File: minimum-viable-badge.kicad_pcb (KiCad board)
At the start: 2 copper layers, 120 x 64 mm, 67 parts, among them J101 EDGE_CONNECTOR, P101 USB, P102 BATTERY, P103 POT_LONG, P104 BUTTON_A, P105 BUTTON_B, P106 POT_SHORT, P107 MECH, P108 MECH, P109 MECH, P301 eInk, Q101 S8050, Q102 S8050, Q201 FDN340P, Q301 IRLML0030TRPBF, SW101 PRGM, SW102 RESET, SW201 ON|OFF, U101 ESP32-WROOM, U102 CP2102, U201 MCP73831, U202 NCP5501

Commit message: Flipped is better.
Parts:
- C101, C102, C103, C104, C105, C106, C107, C201, C202, C203, C204, C301, C302, C303, C304, C305, C306, C307, C308, C309, C310, C311, C312, D101, D201, D202, D203, D301, D302, D303, F101, J101, L301, P101, P102, P107, P108, P109, P301, Q101, Q102, Q201, Q301, R101, R102, R103, R104, R105, R106, R107, R108, R201, R202, R203, R301, R302, SW101, SW102, SW201, U101, U102, U201, U202: moved to B.Cu
- P103, P104, P105, P106: moved to F.Cu
- moved F101 75.9 mm to (52.2, 21.1)
- moved P102 74.1 mm to (45.7, 22.1)
- moved P108 70.3 mm to (25.8, 24.0)
- moved J101 67.1 mm to (82.3, 25.6), turned to 90 degrees
- moved D101 64.5 mm to (52.1, 26.8)
- moved SW102 55.6 mm to (37.3, 31.3)
- moved SW101 51.7 mm to (26.1, 33.2)
- moved U101 50.9 mm to (124.5, 33.6), turned to 315 degrees
- moved P103 44.0 mm to (71.7, 37.1)
- moved C102 41.3 mm to (31.5, 38.5)
- moved R102 41.2 mm to (36.0, 38.5)
- moved P101 41.1 mm to (93.0, 79.6), turned to 90 degrees
- moved R203 39.7 mm to (117.3, 79.0)
- moved L301 39.7 mm to (48.0, 78.9)
- moved C307 39.7 mm to (40.5, 78.9)
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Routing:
- added copper zone on F.Cu, net GND
- removed copper zone on B.Cu, net GND
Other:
- outline, holes or cut-outs redrawn

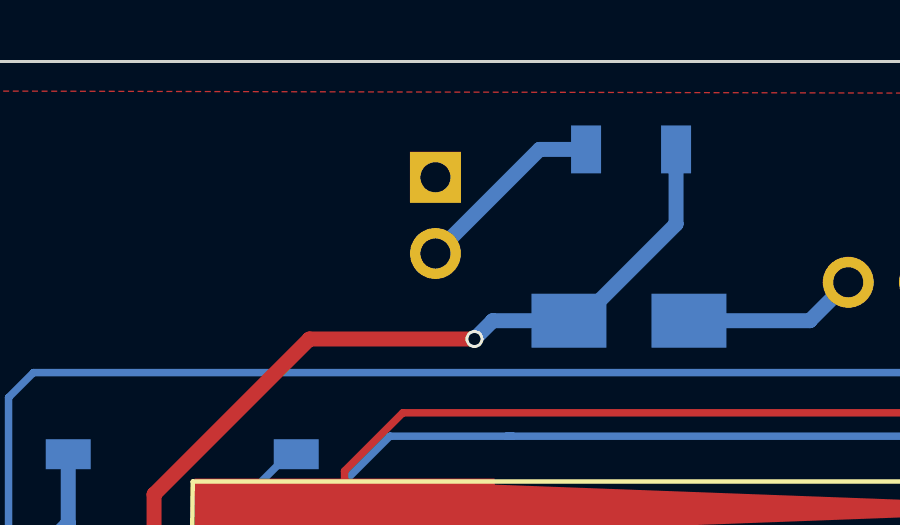
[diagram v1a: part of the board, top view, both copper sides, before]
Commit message: Swap battery connector to JST PH 2.0
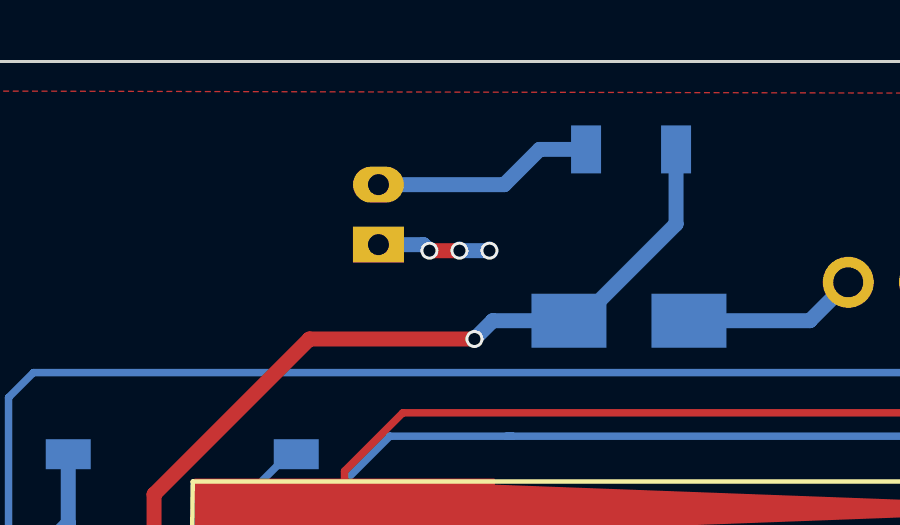
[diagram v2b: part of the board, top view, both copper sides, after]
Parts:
- P102: footprint Pin_Headers:Pin_Header_Angled_1x02_Pitch2.54mm -> Connectors_JST:JST_PH_S2B-PH-K_02x2.00mm_Angled
- moved P102 2.94 mm to (43.8, 24.3), turned to 90 degrees
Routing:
- net GND: track 141.5 -> 145.3 mm, vias 39 -> 42
- net Net-(F101-Pad1): track 6.46 -> 7.41 mm
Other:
- board text added: "+"
- board text added: "-"

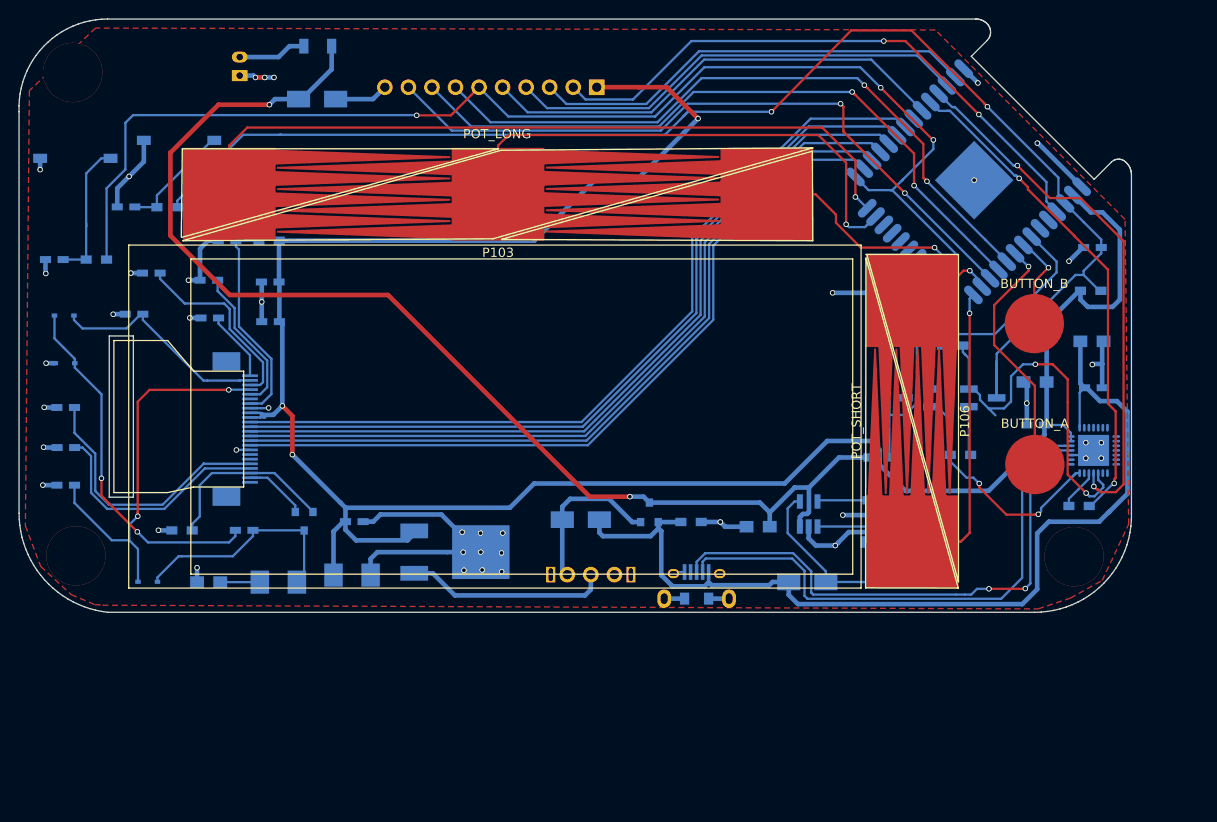
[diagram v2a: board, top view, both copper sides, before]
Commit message: Ground planes, power nets, move bulk cap close to ESP32
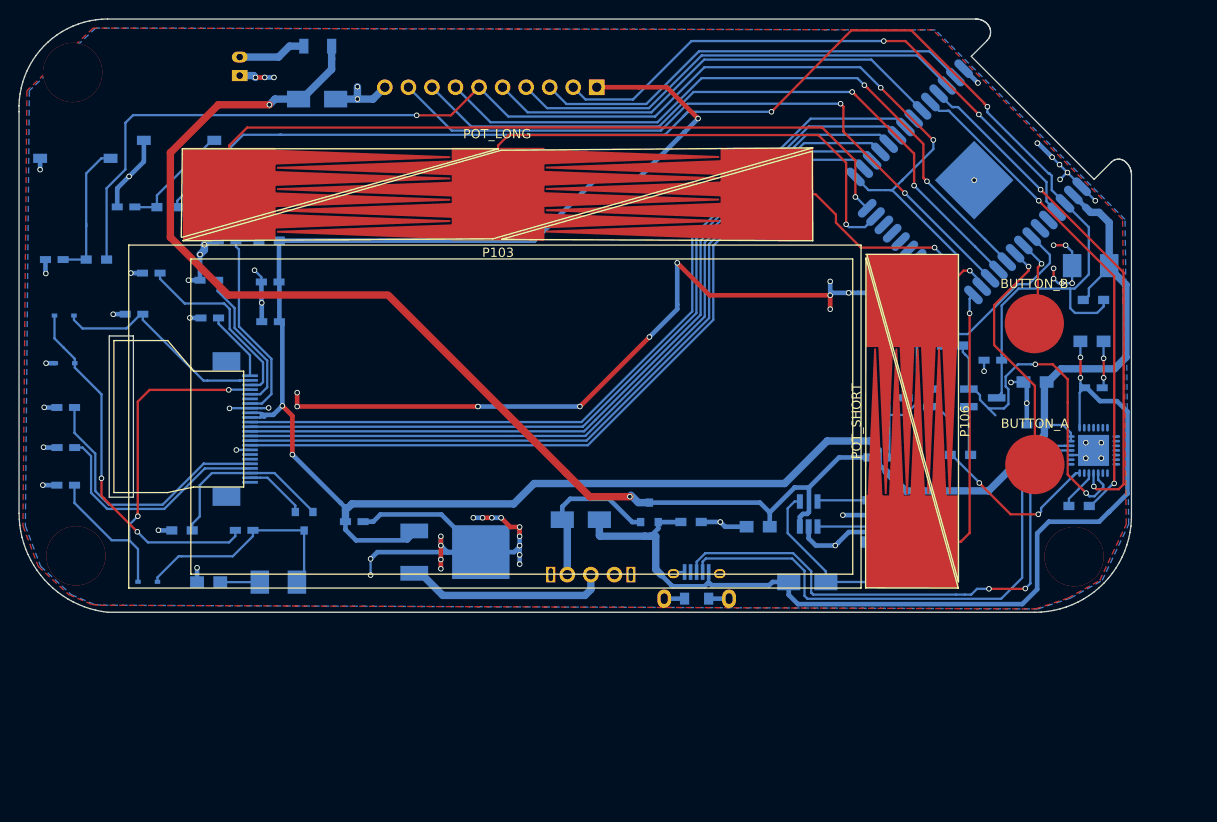
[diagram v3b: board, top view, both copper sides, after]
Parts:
- moved C204 86.4 mm to (135.6, 44.8), turned to 180 degrees
- moved C103 16.2 mm to (125.0, 55.0)
- moved R106 1.03 mm to (135.9, 48.5)
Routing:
- net GND: track 145.3 -> 259.9 mm, vias 42 -> 76
- net /USB_VCC: track 108.2 -> 103.5 mm, vias 0 -> 2
- net +3V3: track 243.6 -> 240.8 mm
- net /EN: track 148.6 -> 151.0 mm
- net /RXD: track 58.1 -> 55.9 mm
- net /BAT_MON: track 47.1 -> 45.5 mm
- net /IO32: track 10.4 -> 9.62 mm
- net /DTR: track 26.4 -> 25.7 mm
- net /RTS: track 39.3 -> 39.9 mm
- added copper zone on B.Cu, net GND
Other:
- net class Default: clearance 0.2 -> 0.15
- rule trace_clearance: 0.2 -> 0.15

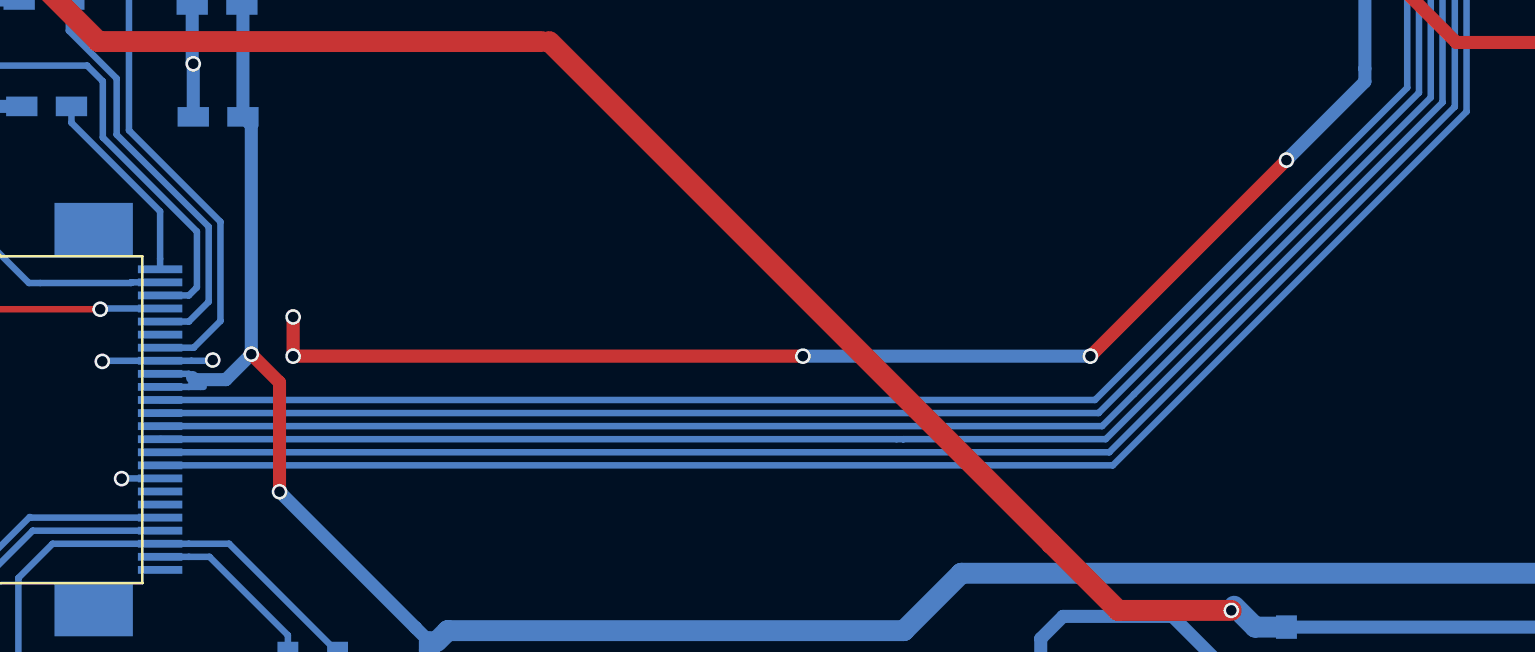
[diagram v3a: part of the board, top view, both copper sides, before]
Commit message: Add missing stitching vias on other side of eink data lines
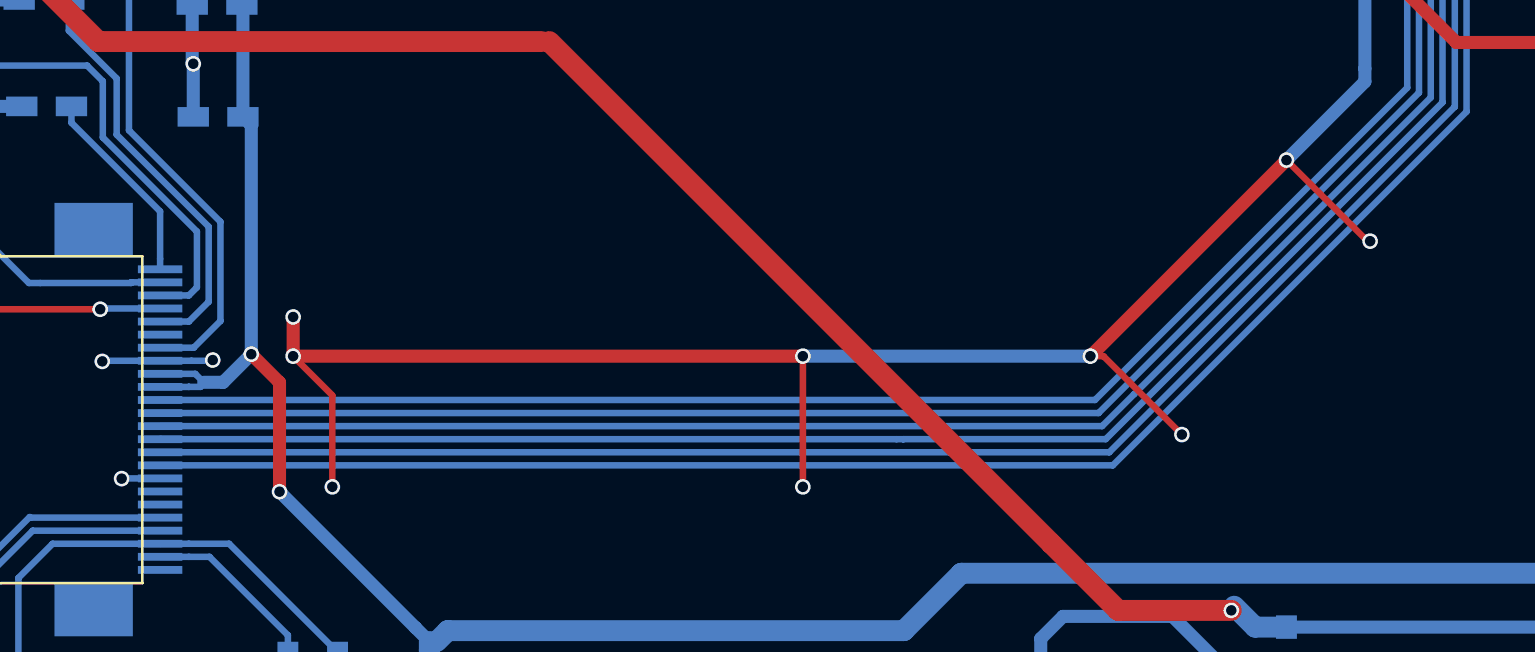
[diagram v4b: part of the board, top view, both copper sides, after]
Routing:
- net GND: track 259.9 -> 279.7 mm, vias 76 -> 80
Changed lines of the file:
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@@
     (links 175)
     (no_connects 0)
-    (area 19.94251 18.144829 140.050001 82.244831)
+    (area 19.94251 14.305544 143.370784 83.776801)
     (thickness 1.6)
     (drawings 174)
-    (tracks 993)
+    (tracks 1003)
     (zones 0)
     (modules 67)
@@
   )
   (setup
-    (last_trace_width 0.25)
+    (last_trace_width 0.5)
     (user_trace_width 0.25)
     (user_trace_width 0.5)
@@
     (visible_elements 7FFFFFFF)
     (pcbplotparams
-      (layerselection 0x110ff_80000001)
+      (layerselection 0x010ff_80000001)
       (usegerberextensions true)
+      (gerberprecision 5)
       (excludeedgelayer true)
       (linewidth 0.100000)
@@
     (tags "capacitor 1210")
     (attr smd)
-    (fp_text reference C204 (at -0.5 -4 180) (layer B.SilkS)
+    (fp_text reference C204 (at 0.1 3.6 180) (layer B.SilkS)
       (effects (font (size 1 1) (thickness 0.15)) (justify mirror))
     )
@@
   (gr_line (start 20 71.514729) (end 20.019876 72.168009) (layer Edge.Cuts) (width 0.1))
   (gr_line (start 20 28.19483) (end 20 71.514729) (layer Edge.Cuts) (width 0.1))
+  (segment (start 48.4 59.92483) (end 47.32483 61) (width 0.5) (layer B.Cu) (net 1))
+  (segment (start 47.32483 61) (end 46.58 61) (width 0.5) (layer B.Cu) (net 1))
+  (segment (start 46.46 61.17483) (end 46.46 61.12) (width 0.25) (layer B.Cu) (net 1))
+  (segment (start 46.46 61.12) (end 46.58 61) (width 0.25) (layer B.Cu) (net 1))
+  (segment (start 44.911714 60.67644) (end 46.25644 60.67644) (width 0.25) (layer B.Cu) (net 1))
+  (segment (start 46.25644 60.67644) (end 46.58 61) (width 0.25) (layer B.Cu) (net 1))
+  (segment (start 46.58 61) (end 46.6 61) (width 0.25) (layer B.Cu) (net 1))
   (segment (start 139.4 46.85) (end 137.6 45.05) (width 0.8) (layer B.Cu) (net 1))
   (segment (start 139.4 54.7) (end 139.4 46.85) (width 0.8) (layer B.Cu) (net 1))
@@
   (via (at 48.4 59.92483) (size 0.6) (drill 0.4) (layers F.Cu B.Cu) (net 1))
   (via (at 49.48 65.18483) (size 0.6) (drill 0.4) (layers F.Cu B.Cu) (net 1))
-  (segment (start 48.4 59.92483) (end 47.4266 60.89823) (width 0.5) (layer B.Cu) (net 1))
-  (segment (start 47.4266 60.89823) (end 46.233504 60.89823) (width 0.5) (layer B.Cu) (net 1))
-  (segment (start 46.233504 60.89823) (end 46.150106 60.814832) (width 0.5) (layer B.Cu) (net 1))
   (segment (start 48.08 46.52483) (end 48.04 46.56483) (width 0.5) (layer B.Cu) (net 1))
   (segment (start 46.013324 61.17483) (end 46.46 61.17483) (width 0.25) (layer B.Cu) (net 1))
-  (segment (start 46.46 61.17483) (end 46.58 61.17483) (width 0.25) (layer B.Cu) (net 1))
-  (segment (start 46.150106 60.814832) (end 46.150106 60.864936) (width 0.25) (layer B.Cu) (net 1))
-  (segment (start 46.150106 60.864936) (end 46.46 61.17483) (width 0.25) (layer B.Cu) (net 1))
-  (segment (start 44.911714 60.67644) (end 46.011714 60.67644) (width 0.25) (layer B.Cu) (net 1))
-  (segment (start 46.011714 60.67644) (end 46.150106 60.814832) (width 0.25) (layer B.Cu) (net 1))
   (segment (start 44.911714 61.17644) (end 46.011714 61.17644) (width 0.25) (layer B.Cu) (net 1))
   (segment (start 46.011714 61.17644) (end 46.013324 61.17483) (width 0.25) (layer B.Cu) (net 1))
@@
   (segment (start 132.62 61.99483) (end 133.46 62.83483) (width 0.25) (layer B.Cu) (net 1))
   (segment (start 133.46 62.83483) (end 133.46 63.23483) (width 0.25) (layer B.Cu) (net 1))
+  (segment (start 50 60) (end 51.5 61.5) (width 0.25) (layer F.Cu) (net 2))
+  (segment (start 51.5 61.5) (end 51.5 65) (width 0.25) (layer F.Cu) (net 2))
+  (via (at 51.5 65) (size 0.6) (drill 0.4) (layers F.Cu B.Cu) (net 2))
+  (segment (start 69.5 60) (end 69.5 65) (width 0.25) (layer F.Cu) (net 2))
+  (via (at 69.5 65) (size 0.6) (drill 0.4) (layers F.Cu B.Cu) (net 2))
+  (segment (start 80.5 60) (end 81 60) (width 0.25) (layer F.Cu) (net 2))
+  (segment (start 81 60) (end 84 63) (width 0.25) (layer F.Cu) (net 2))
+  (via (at 84 63) (size 0.6) (drill 0.4) (layers F.Cu B.Cu) (net 2))
+  (segment (start 88 52.5) (end 91.1 55.6) (width 0.25) (layer F.Cu) (net 2))
+  (segment (start 91.1 55.6) (end 91.2 55.6) (width 0.25) (layer F.Cu) (net 2))
+  (via (at 91.2 55.6) (size 0.6) (drill 0.4) (layers F.Cu B.Cu) (net 2))
   (segment (start 57.92 76.43483) (end 57.92 78.18483) (width 0.25) (layer B.Cu) (net 2))
   (via (at 57.92 78.18483) (size 0.6) (drill 0.4) (layers F.Cu B.Cu) (net 2))
